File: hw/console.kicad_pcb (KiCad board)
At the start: 4 copper layers, 45 x 65 mm, 83 parts, among them J1 Debug Port, J2 USB B Micro, Q1 AP2301, Q2 Si2302CDS, Q3 AP2301, Q4 AP2301, Q5 AP2302, Q6 AP2301, Q7 AP2302, Q8 AP2301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

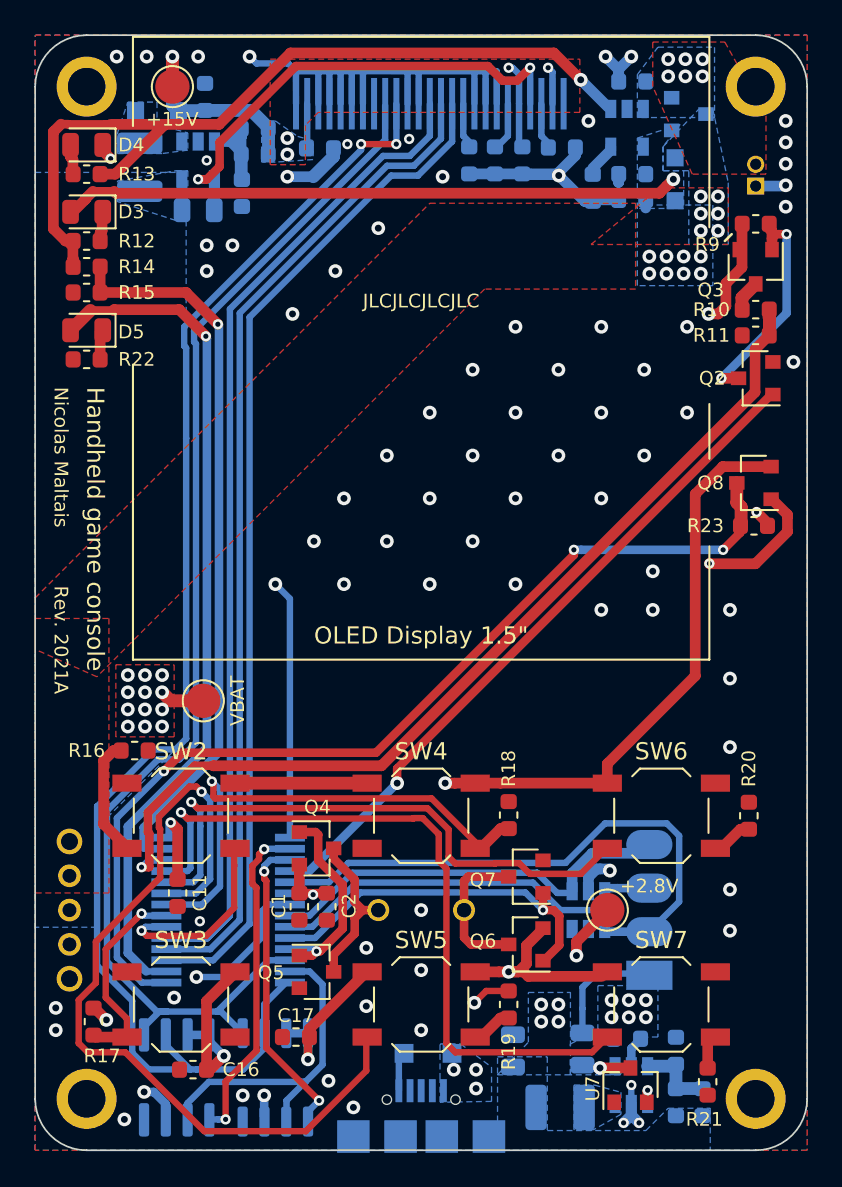
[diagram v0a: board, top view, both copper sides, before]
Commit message: Add missing pull down on buzzer H-bridge, 15V enable
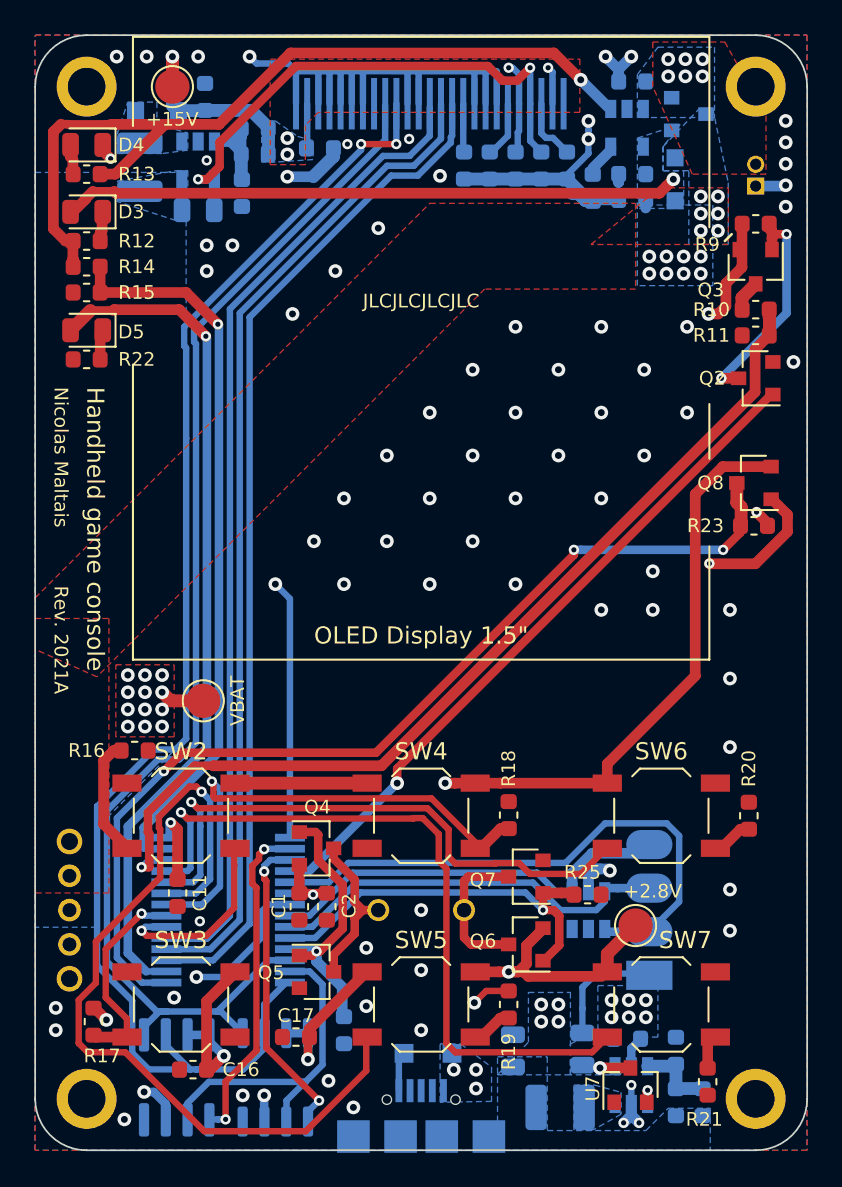
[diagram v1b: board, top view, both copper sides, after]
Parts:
- added R24: 100k, Resistor_SMD:R_0603_1608Metric, B.Cu at (138.0, 118.0)
- added R25: 100k, Resistor_SMD:R_0603_1608Metric, F.Cu at (152.2, 110.1)
- added R26: 100k, Resistor_SMD:R_0603_1608Metric, B.Cu at (149.5, 67.6)
- R1: value 380k -> 330k
- R10: value 16k -> 18k
- R11: value 20k -> 22k
- R14: value 43k -> 20k
- R15: value 56k -> 27k
- R2: value 120k -> 91k
- moved TP2 1.88 mm to (155.0, 111.9)
- moved C15 1.09 mm to (151.0, 67.6), turned to 90 degrees
- moved C13 0.50 mm to (148.0, 67.6)
- moved C14 0.42 mm to (146.5, 67.6)
- moved R8 0.42 mm to (145.0, 67.6)
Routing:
- net /BUZZER+: track 12.1 -> 16.6 mm
- net /EN_15V: track 26.7 -> 29.7 mm
- net /BUZZER-: track 21.4 -> 23.2 mm
- net GND: track 101.0 -> 102.8 mm
- net Net-(C15-Pad2): track 2.43 -> 3.67 mm
- net Net-(C14-Pad2): track 2.62 -> 3.32 mm
- net +2V8: track 92.2 -> 92.6 mm, vias 14 -> 13

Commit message: PCB improvements & enclosure
- Change revision to 2021B
- Larger battery connector holes
- Change buzzer to 8 ohm speaker
- Add enclosure CAD files
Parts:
- removed BZ1: Buzzer, console:XDCR_PS1240P02CT3
- added LS1: Speaker, console:Speaker, B.Cu at (142.5, 111.0)
- Q2: value Si2302CDS -> AP2302
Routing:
- net GND: track 102.8 -> 105.7 mm
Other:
- board text added: "Rev. 2021B"
- board text removed: "Rev. 2021A"

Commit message: Migrate to KiCad 6
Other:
- net class Default removed

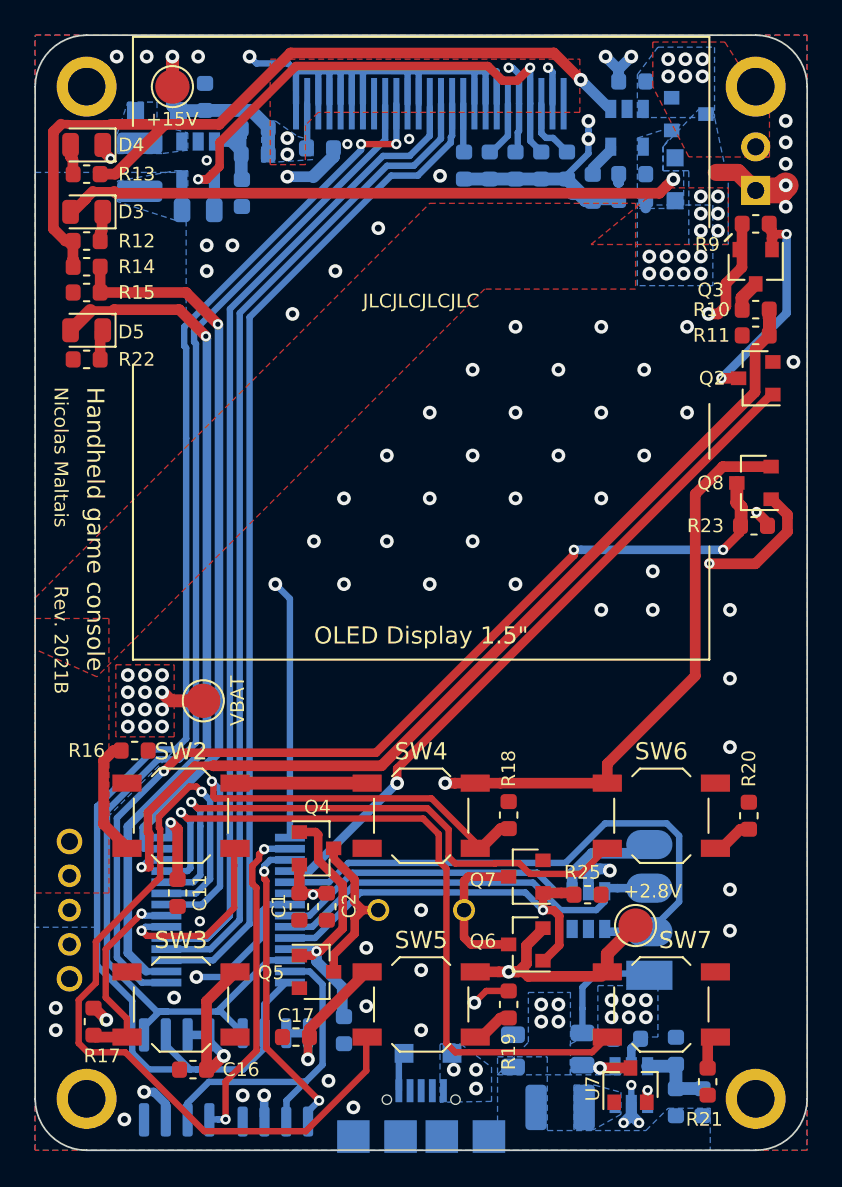
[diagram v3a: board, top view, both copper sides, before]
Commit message: PCB: removed reset monitor
Causes drop in power when USB is disconnected and not really necessary.
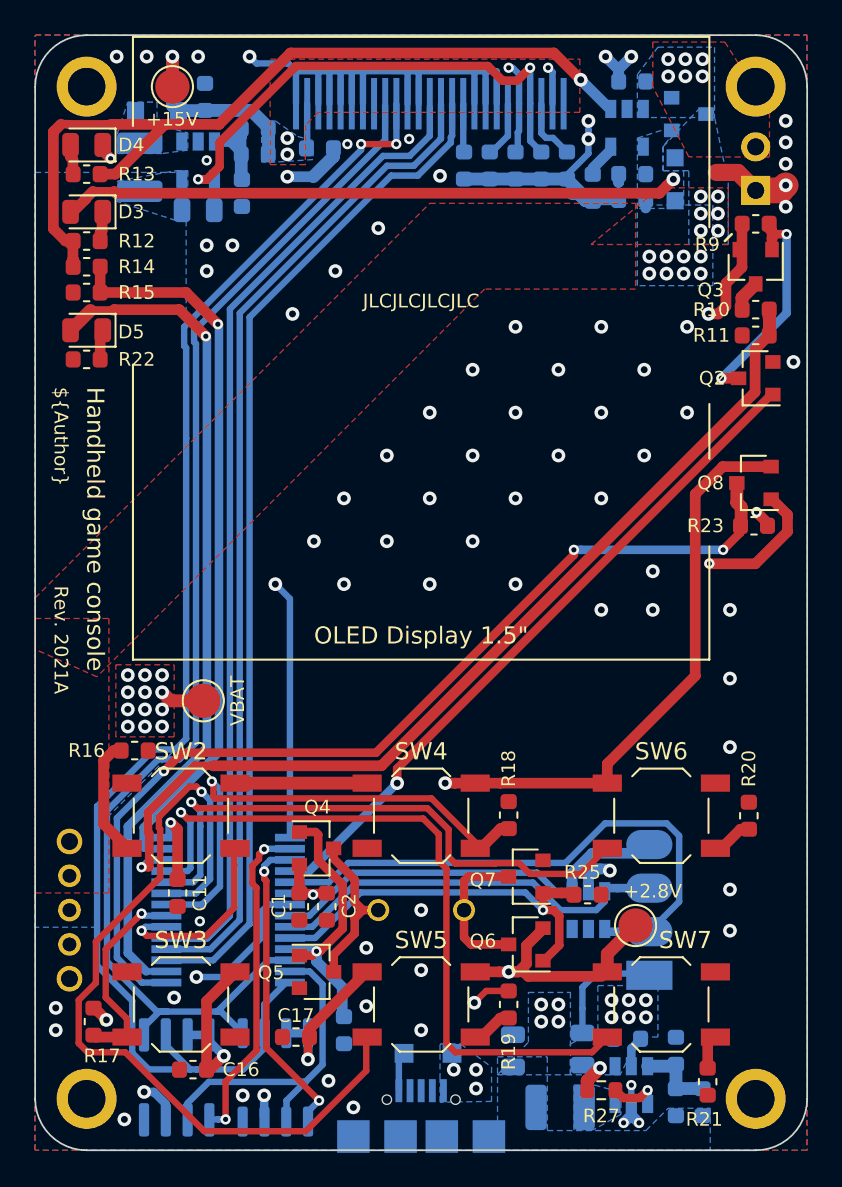
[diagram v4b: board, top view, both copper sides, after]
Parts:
- removed U7: SE809, Package_TO_SOT_SMD:SOT-23
- added R27: 100k, Resistor_SMD:R_0603_1608Metric, F.Cu at (153.0, 121.5)
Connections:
- D7 pad 5: Net-(D7-Pad5) -> unconnected-(D7-Pad5)
- D7 pad 6: Net-(D7-Pad6) -> unconnected-(D7-Pad6)
- DS1 pad 18: Net-(DS1-Pad18) -> unconnected-(DS1-Pad18)
- J2 pad 2: Net-(J2-Pad2) -> unconnected-(J2-Pad2)
- J2 pad 3: Net-(J2-Pad3) -> unconnected-(J2-Pad3)
- J2 pad 4: Net-(J2-Pad4) -> unconnected-(J2-Pad4)
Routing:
- net Net-(R27-Pad2): track 1.42 -> 3.02 mm
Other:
- board text added: "${Author}"
- board text added: "${Title}"
- board text added: "Rev. ${Revision}"
- board text removed: "Handheld game console"
- board text removed: "Nicolas Maltais"
- board text removed: "Rev. 2021B"

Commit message: PCB: removed power monitor
Far from enough capacity on board to ever be useful.
Power monitor was envisioned to prevent EEPROM corruption. This was instead prevented with atomic operation (copy before write).
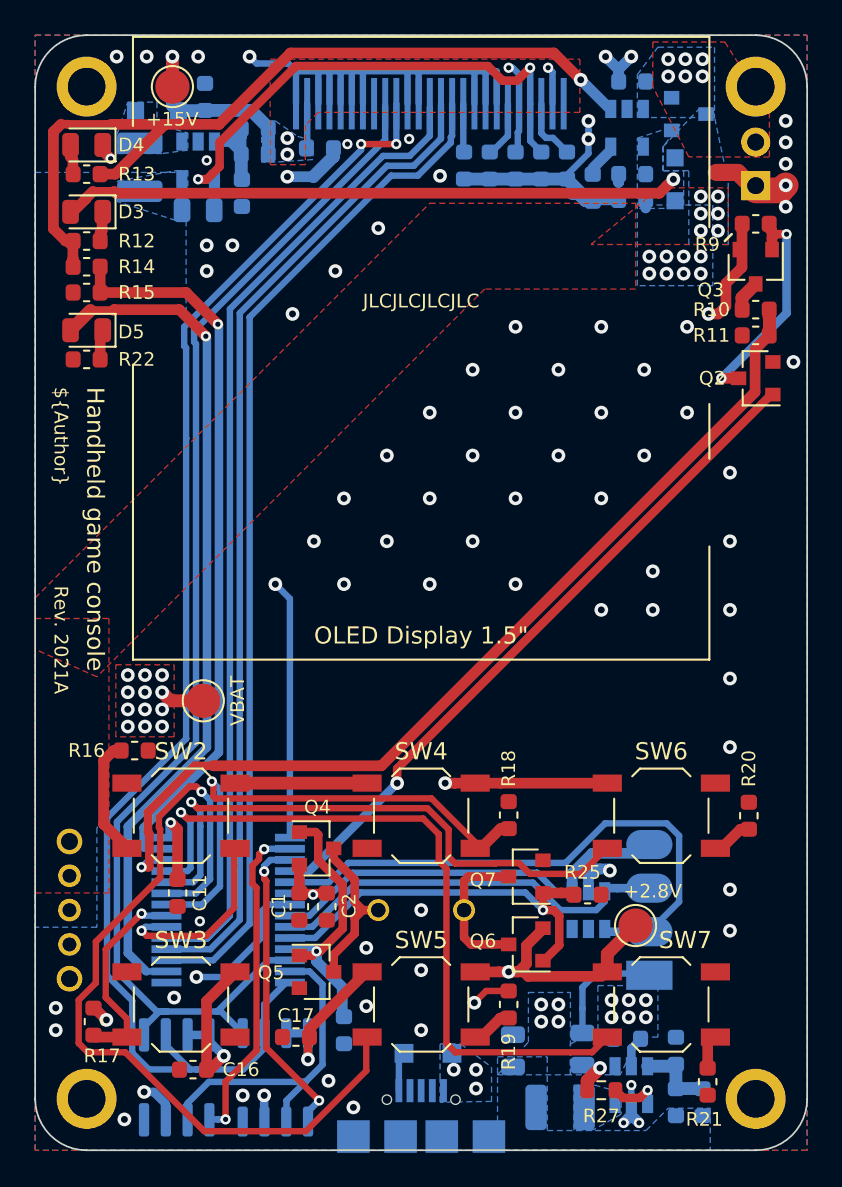
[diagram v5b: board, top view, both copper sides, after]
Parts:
- removed Q8: AP2301, Package_TO_SOT_SMD:SOT-23
- removed R23: 100k, Resistor_SMD:R_0603_1608Metric
- moved BT1 0.28 mm to (162.0, 67.2)
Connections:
- U1 pad 1: /POWER_MON -> unconnected-(U1-Pad1)
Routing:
- net /POWER_MON: track 57.2 -> 0.00 mm, vias 3 -> 0
- net +2V8: track 92.6 -> 68.6 mm
- net VBAT: track 18.2 -> 10.5 mm, vias 21 -> 20
- net /SCK: track 80.0 -> 78.8 mm
- net /MOSI: track 74.4 -> 73.2 mm
- net GND: track 105.7 -> 104.8 mm, vias 80 -> 81
